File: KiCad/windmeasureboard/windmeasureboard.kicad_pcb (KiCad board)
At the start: 2 copper layers, 3 parts, among them J1 ESQ-120-XX-X-D-XX, U1 TMS320F28379DPTPS

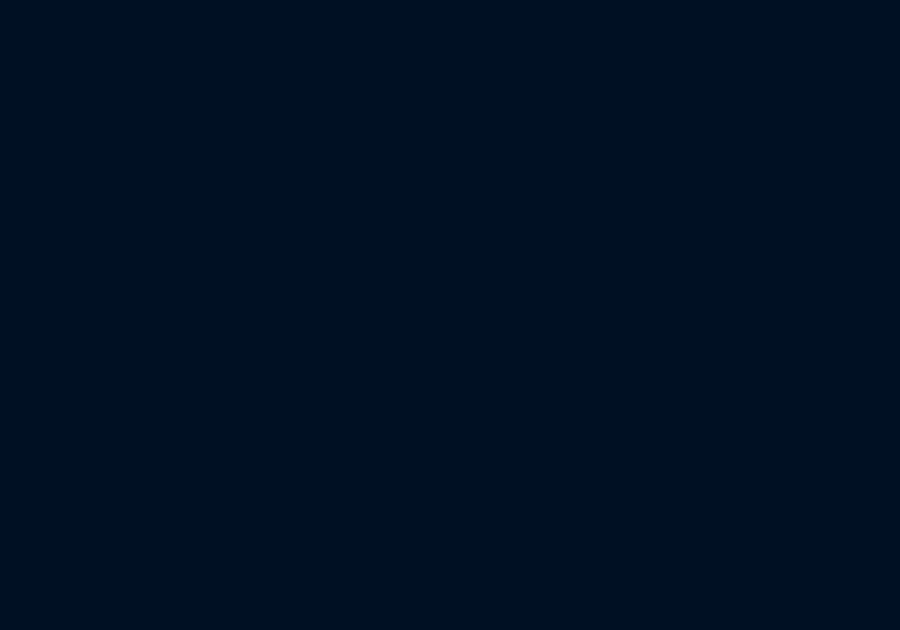
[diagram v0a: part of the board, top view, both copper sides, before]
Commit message: push before i swap out diodes for mosfets
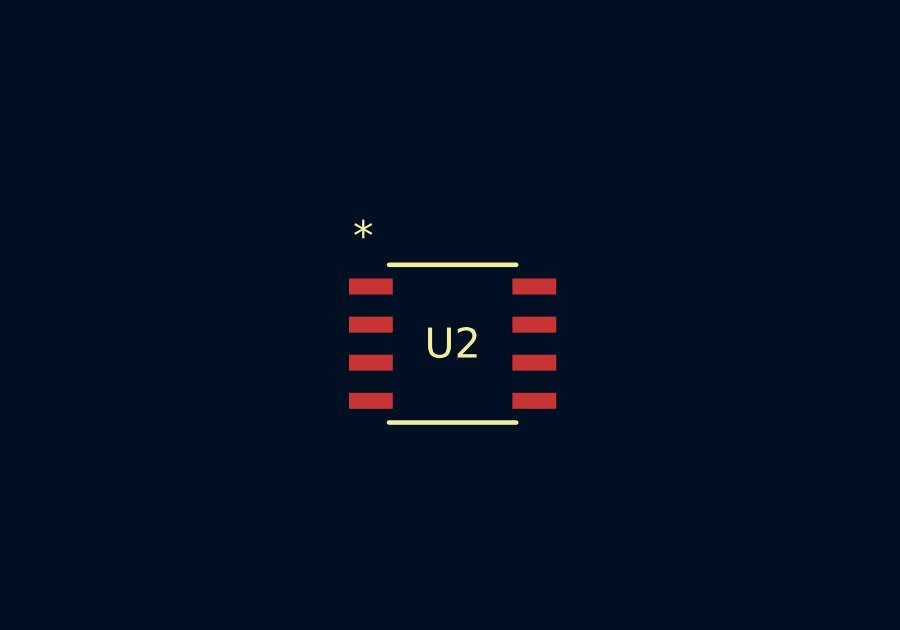
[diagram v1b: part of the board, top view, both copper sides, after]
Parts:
- added U2: LT1573IS8-PBF, footprints:SO-8_S_LIT, F.Cu at (131.9, 121.6)
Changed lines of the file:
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@@
   (net 213 "unconnected-(U1-Pad33)")
   (net 214 "unconnected-(U1-Pad45)")
+  (net 215 "unconnected-(U2-Pad1)")
+  (net 216 "unconnected-(U2-Pad2)")
+  (net 217 "unconnected-(U2-Pad3)")
+  (net 218 "unconnected-(U2-Pad4)")
+  (net 219 "unconnected-(U2-Pad5)")
+  (net 220 "unconnected-(U2-Pad6)")
+  (net 221 "unconnected-(U2-Pad7)")
+  (net 222 "unconnected-(U2-Pad8)")
   (footprint "footprints:PTP0176F_N" (layer "F.Cu")
     (at 133.532198 87.324401)
@@
       (net 1 "GND") (pinfunction "40") (pintype "passive") (solder_mask_margin 0.102))
   )
+  (footprint "footprints:SO-8_S_LIT" (layer "F.Cu")
+    (at 131.8514 121.6406)
+    (tags "LT1573IS8-PBF ")
+    (property "Sheetfile" "windmeasureboard.kicad_sch")
+    (property "Sheetname" "")
+    (attr smd)
+    (fp_text reference "U2" (at 0 0 unlocked) (layer "F.SilkS")
+      (effects (font (size 1 1) (thickness 0.15)))
+    )
+    (fp_text value "LT1573IS8-PBF" (at 0 0 unlocked) (layer "F.Fab")
+      (effects (font (size 1 1) (thickness 0.15)))
+    )
+    (fp_text user "*" (at -2.97815 -3.5814) (layer "F.SilkS")
+      (effects (font (size 1 1) (thickness 0.15)))
+    )
+    (fp_text user "*" (at -2.97815 -3.5814 unlocked) (layer "F.SilkS")
+      (effects (font (size 1 1) (thickness 0.15)))
+    )
+    (fp_text user "*" (at -1.6129 -2.4257 unlocked) (layer "F.Fab")
+      (effects (font (size 1 1) (thickness 0.15)))
+    )
+    (fp_text user "${REFERENCE}" (at 0 0 unlocked) (layer "F.Fab")
+      (effects (font (size 1 1) (thickness 0.15)))
+    )
+    (fp_text user "*" (at -1.6129 -2.4257) (layer "F.Fab")
+      (effects (font (size 1 1) (thickness 0.15)))
+    )
+    (fp_line (start 2.1209 -2.6289) (end -2.1209 -2.6289) (layer "F.SilkS") (width 0.1524))
+    (fp_line (start -2.1209 2.6289) (end 2.1209 2.6289) (layer "F.SilkS") (width 0.1524))
+    (fp_line (start -3.7084 -2.4257) (end -2.2479 -2.4257) (layer "F.CrtYd") (width 0.1524))
+    (fp_line (start 2.2479 2.4257) (end 2.2479 2.7559) (layer "F.CrtYd") (width 0.1524))
+    (fp_line (start -2.2479 2.7559) (end -2.2479 2.4257) (layer "F.CrtYd") (width 0.1524))
+    (fp_line (start 2.2479 -2.7559) (end 2.2479 -2.4257) (layer "F.CrtYd") (width 0.1524))
+    (fp_line (start -2.2479 -2.4257) (end -2.2479 -2.7559) (layer "F.CrtYd") (width 0.1524))
+    (fp_line (start 3.7084 2.4257) (end 2.2479 2.4257) (layer "F.CrtYd") (width 0.1524))
+    (fp_line (start -3.7084 2.4257) (end -2.2479 2.4257) (layer "F.CrtYd") (width 0.1524))
+    (fp_line (start 3.7084 -2.4257) (end 3.7084 2.4257) (layer "F.CrtYd") (width 0.1524))
+    (fp_line (start -3.7084 2.4257) (end -3.7084 -2.4257) (layer "F.CrtYd") (width 0.1524))
+    (fp_line (start 3.7084 -2.4257) (end 2.2479 -2.4257) (layer "F.CrtYd") (width 0.1524))
+    (fp_line (start 2.2479 2.7559) (end -2.2479 2.7559) (layer "F.CrtYd") (width 0.1524))
+    (fp_line (start -2.2479 -2.7559) (end 2.2479 -2.7559) (layer "F.CrtYd") (width 0.1524))
+    (fp_line (start 1.9939 -1.6637) (end 3.0988 -1.6637) (layer "F.Fab") (width 0.0254))
+    (fp_line (start -1.9939 0.8763) (end -1.9939 0.3937) (layer "F.Fab") (width 0.0254))
+    (fp_line (start 3.0988 0.8763) (end 3.0988 0.3937) (layer "F.Fab") (width 0.0254))
+    (fp_line (start -3.0988 1.6637) (end -3.0988 2.1463) (layer "F.Fab") (width 0.0254))
+    (fp_line (start 1.9939 1.6637) (end 1.9939 2.1463) (layer "F.Fab") (width 0.0254))
+    (fp_line (start -1.9939 -2.1463) (end -3.0988 -2.1463) (layer "F.Fab") (width 0.0254))
+    (fp_line (start -1.9939 -2.5019) (end -1.9939 2.5019) (layer "F.Fab") (width 0.0254))
+    (fp_line (start -3.0988 -0.3937) (end -1.9939 -0.3937) (layer "F.Fab") (width 0.0254))
+    (fp_line (start -1.9939 -1.6637) (end -1.9939 -2.1463) (layer "F.Fab") (width 0.0254))
+    (fp_line (start 1.9939 -2.1463) (end 1.9939 -1.6637) (layer "F.Fab") (width 0.0254))
+    (fp_line (start -1.9939 1.6637) (end -3.0988 1.6637) (layer "F.Fab") (width 0.0254))
+    (fp_line (start -3.0988 2.1463) (end -1.9939 2.1463) (layer "F.Fab") (width 0.0254))
+    (fp_line (start 1.9939 2.1463) (end 3.0988 2.1463) (layer "F.Fab") (width 0.0254))
+    (fp_line (start 1.9939 0.8763) (end 3.0988 0.8763) (layer "F.Fab") (width 0.0254))
+    (fp_line (start -1.9939 2.5019) (end 1.9939 2.5019) (layer "F.Fab") (width 0.0254))
+    (fp_line (start -3.0988 0.3937) (end -3.0988 0.8763) (layer "F.Fab") (width 0.0254))
+    (fp_line (start 3.0988 -0.8763) (end 1.9939 -0.8763) (layer "F.Fab") (width 0.0254))
+    (fp_line (start -1.9939 -0.3937) (end -1.9939 -0.8763) (layer "F.Fab") (width 0.0254))
+    (fp_line (start 3.0988 1.6637) (end 1.9939 1.6637) (layer "F.Fab") (width 0.0254))
+    (fp_line (start 3.0988 -2.1463) (end 1.9939 -2.1463) (layer "F.Fab") (width 0.0254))
+    (fp_line (start 1.9939 0.3937) (end 1.9939 0.8763) (layer "F.Fab") (width 0.0254))
+    (fp_line (start -3.0988 -0.8763) (end -3.0988 -0.3937) (layer "F.Fab") (width 0.0254))
+    (fp_line (start -3.0988 0.8763) (end -1.9939 0.8763) (layer "F.Fab") (width 0.0254))
+    (fp_line (start -1.9939 2.1463) (end -1.9939 1.6637) (layer "F.Fab") (width 0.0254))
+    (fp_line (start -1.9939 0.3937) (end -3.0988 0.3937) (layer "F.Fab") (width 0.0254))
+    (fp_line (start 1.9939 -0.3937) (end 3.0988 -0.3937) (layer "F.Fab") (width 0.0254))
+    (fp_line (start 1.9939 -2.5019) (end -1.9939 -2.5019) (layer "F.Fab") (width 0.0254))
+    (fp_line (start 3.0988 -0.3937) (end 3.0988 -0.8763) (layer "F.Fab") (width 0.0254))
+    (fp_line (start 1.9939 -0.8763) (end 1.9939 -0.3937) (layer "F.Fab") (width 0.0254))
+    (fp_line (start -3.0988 -1.6637) (end -1.9939 -1.6637) (layer "F.Fab") (width 0.0254))
+    (fp_line (start 3.0988 -1.6637) (end 3.0988 -2.1463) (layer "F.Fab") (width 0.0254))
+    (fp_line (start -1.9939 -0.8763) (end -3.0988 -0.8763) (layer "F.Fab") (width 0.0254))
+    (fp_line (start 1.9939 2.5019) (end 1.9939 -2.5019) (layer "F.Fab") (width 0.0254))
+    (fp_line (start -3.0988 -2.1463) (end -3.0988 -1.6637) (layer "F.Fab") (width 0.0254))
+    (fp_line (start 3.0988 0.3937) (end 1.9939 0.3937) (layer "F.Fab") (width 0.0254))
+    (fp_line (start 3.0988 2.1463) (end 3.0988 1.6637) (layer "F.Fab") (width 0.0254))
+    (fp_arc (start 0.3048 -2.5019) (mid 0 -2.1971) (end -0.3048 -2.5019) (layer "F.Fab") (width 0.0254))
+    (pad "1" smd rect (at -2.72415 -1.905) (size 1.4605 0.5334) (layers "F.Cu" "F.Paste" "F.Mask")
+      (net 215 "unconnected-(U2-Pad1)") (pinfunction "FB") (pintype "input"))
+    (pad "2" smd rect (at -2.72415 -0.635) (size 1.4605 0.5334) (layers "F.Cu" "F.Paste" "F.Mask")
+      (net 216 "unconnected-(U2-Pad2)") (pinfunction "LATCH") (pintype "unspecified"))
+    (pad "3" smd rect (at -2.72415 0.635) (size 1.4605 0.5334) (layers "F.Cu" "F.Paste" "F.Mask")
+      (net 217 "unconnected-(U2-Pad3)") (pinfunction "SHDN") (pintype "output"))
+    (pad "4" smd rect (at -2.72415 1.905) (size 1.4605 0.5334) (layers "F.Cu" "F.Paste" "F.Mask")
+      (net 218 "unconnected-(U2-Pad4)") (pinfunction "GND") (pintype "power_in"))
+    (pad "5" smd rect (at 2.72415 1.905) (size 1.4605 0.5334) (layers "F.Cu" "F.Paste" "F.Mask")
+      (net 219 "unconnected-(U2-Pad5)") (pinfunction "DRIVE") (pintype "unspecified"))
+    (pad "6" smd rect (at 2.72415 0.635) (size 1.4605 0.5334) (layers "F.Cu" "F.Paste" "F.Mask")
+      (net 220 "unconnected-(U2-Pad6)") (pinfunction "VIN") (pintype "input"))
+    (pad "7" smd rect (at 2.72415 -0.635) (size 1.4605 0.5334) (layers "F.Cu" "F.Paste" "F.Mask")
+      (net 221 "unconnected-(U2-Pad7)") (pinfunction "VOUT") (pintype "output"))
+    (pad "8" smd rect (at 2.72415 -1.905) (size 1.4605 0.5334) (layers "F.Cu" "F.Paste" "F.Mask")
+      (net 222 "unconnected-(U2-Pad8)") (pinfunction "COMP") (pintype "unspecified"))
+  )
   (footprint "footprints:CAPC3225X270N" (layer "F.Cu")

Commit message: worked on measure board
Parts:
- removed C1: GRM32EC72A106KE05L, footprints:CAPC3225X270N
- added LED1: XZMG56W, footprints:LED_XZMG56W_SLD, F.Cu at (125.0, 70.5)
- added LED2: XZMG56W, footprints:LED_XZMG56W_SLD, F.Cu at (121.1, 70.5)
- added LED3: XZMG56W, footprints:LED_XZMG56W_SLD, F.Cu at (117.2, 70.5)
- added LED4: XZMG56W, footprints:LED_XZMG56W_SLD, F.Cu at (113.1, 70.5)
- added LED5: XZMG56W, footprints:LED_XZMG56W_SLD, F.Cu at (109.1, 70.5)
- added LED6: XZMG56W, footprints:LED_XZMG56W_SLD, F.Cu at (105.1, 70.5)
- U1: value TMS320F28379DPTPS -> ESP32-S2-DEVKITC-1; footprint footprints:PTP0176F_N -> footprints:MODULE_ESP32-S2-DEVKITC-1
- U2: value LT1573IS8-PBF -> LM1084ISX-5.0_NOPB; footprint footprints:SO-8_S_LIT -> footprints:TS3B
- moved J1 58.1 mm to (130.0, 86.0)
- moved U2 56.4 mm to (165.6, 76.4)
- moved U1 37.8 mm to (131.8, 49.6), turned to 90 degrees
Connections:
- J1 pad 04: PhaseC- -> unconnected-(J1-Pad04)
- J1 pad 05: Brake_sig -> unconnected-(J1-Pad05)
- J1 pad 06: PhaseB- -> PhaseC-
- J1 pad 08: PhaseA- -> unconnected-(J1-Pad08)
- J1 pad 10: unconnected-(J1-Pad10) -> PhaseB-
- J1 pad 13: Shunt1 -> Brake_Q4
- J1 pad 14: unconnected-(J1-Pad14) -> PhaseA-
- J1 pad 15: Shunt2 -> Brake_Q1
- J1 pad 17: unconnected-(J1-Pad17) -> Brake_Q3
- J1 pad 19: unconnected-(J1-Pad19) -> Brake_Q2
- J1 pad 21: unconnected-(J1-Pad21) -> Brake_Q5
- J1 pad 23: unconnected-(J1-Pad23) -> Brake_Q6
- J1 pad 25: unconnected-(J1-Pad25) -> Shunt1
- J1 pad 26: unconnected-(J1-Pad26) -> PowerSW2
- J1 pad 27: unconnected-(J1-Pad27) -> Shunt2
- J1 pad 28: PowerSW2 -> PowerSW1
- J1 pad 29: unconnected-(J1-Pad29) -> Vdrive
- J1 pad 30: PowerSW1 -> Shunt8
- J1 pad 31: Vdrive -> PWM_sig
- J1 pad 32: Shunt8 -> Shunt7
- J1 pad 33: PWM_sig -> Shunt3
- J1 pad 34: Shunt7 -> unconnected-(J1-Pad34)
- J1 pad 35: Shunt3 -> Shunt4
- J1 pad 36: Shunt6 -> Shunt5
- J1 pad 37: Shunt4 -> unconnected-(J1-Pad37)
- J1 pad 38: Shunt5 -> unconnected-(J1-Pad38)
- J1 pad 40: GND -> Shunt6
- U2 pad 1: unconnected-(U2-Pad1) -> GND
- U2 pad 2: unconnected-(U2-Pad2) -> Vsupp
- U2 pad 3: unconnected-(U2-Pad3) -> Shunt6
- U2 pad 4: unconnected-(U2-Pad4) -> Shunt6
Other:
- board outline added: 103.8 x 61.2 mm
- board text added: "(VSupp)"
- board text added: "GND"
- board text added: "NC"
- board text added: "P1Out"
- board text added: "P2Out"
- board text added: "PGND"
- board text added: "PWM"
- board text added: "P_SW1"
- board text added: "P_SW2"
- board text added: "PhaseA"
- board text added: "PhaseA-"
- board text added: "PhaseB"
- board text added: "PhaseB-"
- board text added: "PhaseC"
- board text added: "PhaseC-"
- board text added: "Shunt1"
- board text added: "Shunt2"
- board text added: "Shunt3"
- board text added: "Shunt4"
- board text added: "Shunt5"
- board text added: "Shunt7"
- board text added: "Vdrive"
- board text added: "WMB V.1.0 K.Q"
- board text added: "brakeQ1"
- board text added: "brakeQ2"
- board text added: "brakeQ3"
- board text added: "brakeQ4"
- board text added: "brakeQ5"
- board text added: "brakeQ6"

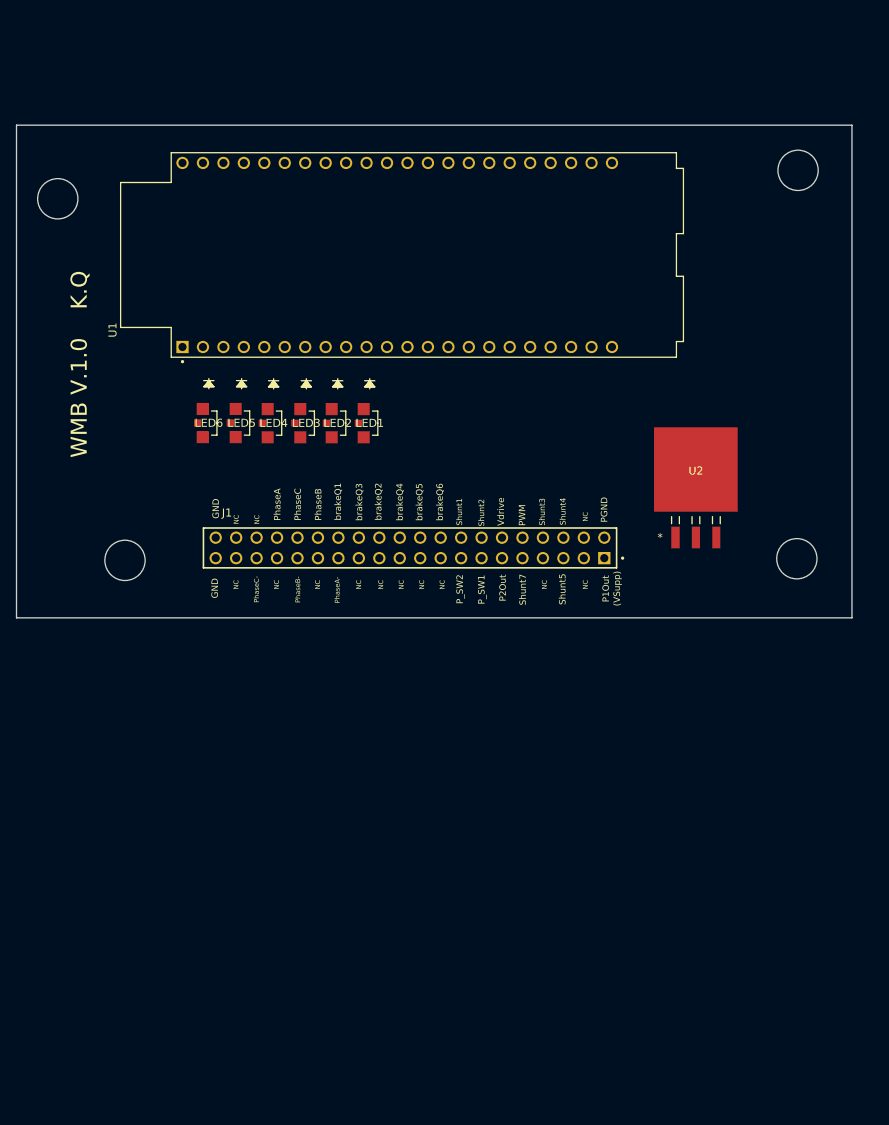
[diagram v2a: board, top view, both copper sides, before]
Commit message: V1 Measure Board Finished
Also started manual data collection for turbine and started updating files to kicad V7
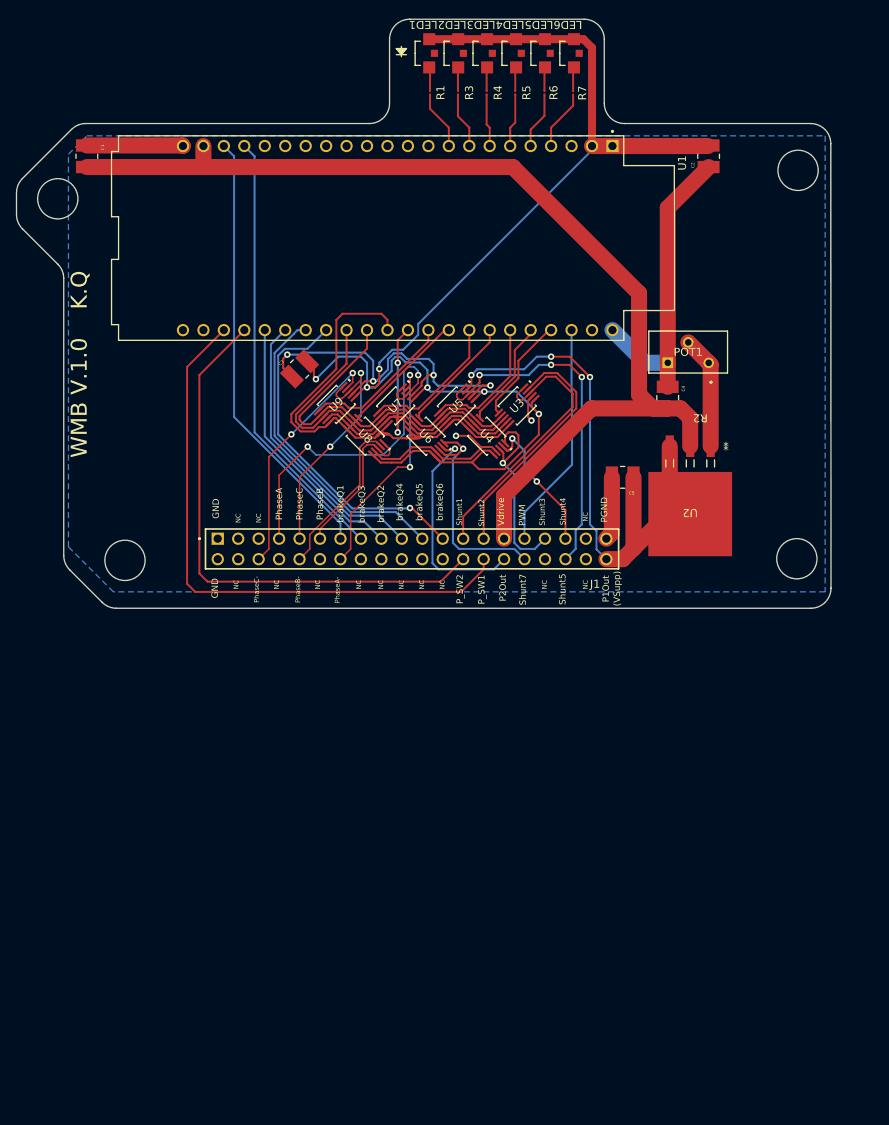
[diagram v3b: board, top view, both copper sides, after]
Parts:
- added C1: GRM32EC72A106KE05L, footprints:CAPC3225X270N, F.Cu at (89.9, 37.3)
- added C2: GRM32EC72A106KE05L, footprints:CAPC3225X270N, F.Cu at (167.1, 37.3)
- added C3: GRM32EC72A106KE05L, footprints:CAPC3225X270N, F.Cu at (116.3, 63.8)
- added C4: GRM32EC72A106KE05L, footprints:CAPC3225X270N, F.Cu at (162.1, 67.3)
- added C5: GRM32EC72A106KE05L, footprints:CAPC3225X270N, F.Cu at (156.5, 77.2)
- added POT1: 3296Y-1-502LF, footprints:POT_3296Y, F.Cu at (162.1, 63.0)
- added R1: ERJXGNJ560Y, footprints:ERJXGN_RCD, F.Cu at (132.5, 29.4)
- added R2: CRCW04021K00FKED, footprints:RES_CRCW_0402, F.Cu at (166.1, 69.8)
- added R3: ERJXGNJ560Y, footprints:ERJXGN_RCD, F.Cu at (136.0, 29.4)
- added R4: ERJXGNJ560Y, footprints:ERJXGN_RCD, F.Cu at (139.6, 29.4)
- added R5: ERJXGNJ560Y, footprints:ERJXGN_RCD, F.Cu at (143.1, 29.4)
- added R6: ERJXGNJ560Y, footprints:ERJXGN_RCD, F.Cu at (146.7, 29.4)
- added R7: ERJXGNJ560Y, footprints:ERJXGN_RCD, F.Cu at (150.3, 29.5)
- added U3: INA229AIDGSR, footprints:VSSOP10_DGS_TEX, F.Cu at (143.4, 68.3)
- added U4: INA229AIDGSR, footprints:VSSOP10_DGS_TEX, F.Cu at (139.6, 72.1)
- added U5: INA229AIDGSR, footprints:VSSOP10_DGS_TEX, F.Cu at (135.8, 68.3)
- added U6: INA229AIDGSR, footprints:VSSOP10_DGS_TEX, F.Cu at (132.0, 72.1)
- added U7: INA229AIDGSR, footprints:VSSOP10_DGS_TEX, F.Cu at (128.3, 68.3)
- added U8: INA229AIDGSR, footprints:VSSOP10_DGS_TEX, F.Cu at (124.5, 72.1)
- added U9: INA229AIDGSR, footprints:VSSOP10_DGS_TEX, F.Cu at (120.9, 68.2)
- moved LED6 64.0 mm to (149.7, 24.6), turned to 180 degrees
- moved LED5 58.9 mm to (146.1, 24.6), turned to 180 degrees
- moved LED4 54.5 mm to (142.5, 24.6), turned to 180 degrees
- moved LED3 50.8 mm to (138.9, 24.6), turned to 180 degrees
- moved LED2 48.1 mm to (135.3, 24.6), turned to 180 degrees
- moved LED1 46.4 mm to (131.7, 24.6), turned to 180 degrees
- moved U1 6.87 mm to (125.2, 47.5), turned to -90 degrees
- moved U2 5.27 mm to (164.8, 81.6), turned to 180 degrees
- moved J1 0.28 mm to (130.3, 86.1), turned to 180 degrees
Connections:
- LED1 pad 1: LED1 -> Net-(LED1-Pad1)
- LED2 pad 1: LED2 -> Net-(LED2-Pad1)
- LED3 pad 1: LED3 -> Net-(LED3-Pad1)
- LED4 pad 1: LED4 -> Net-(LED4-Pad1)
- LED5 pad 1: LED5 -> Net-(LED5-Pad1)
- LED6 pad 1: LED6 -> Net-(LED6-Pad1)
- U1 pad J1_19: unconnected-(U1-PadJ1_19) -> Brake_Q1
- U1 pad J1_2: LED6 -> V3.3+
- U1 pad J1_20: unconnected-(U1-PadJ1_20) -> Brake_Q4
- U1 pad J1_21: Vsupp -> Vdrive
- U1 pad J1_3: LED5 -> unconnected-(U1-EN-PadJ1_3)
- U1 pad J1_4: LED4 -> LED6
- U1 pad J1_5: LED3 -> LED5
- U1 pad J1_6: LED2 -> LED4
- U1 pad J1_7: LED1 -> LED3
- U1 pad J1_8: unconnected-(U1-PadJ1_8) -> LED2
- U1 pad J1_9: unconnected-(U1-PadJ1_9) -> LED1
- U1 pad J3_10: unconnected-(U1-PadJ3_10) -> /measurement chips/CS7
- U1 pad J3_11: unconnected-(U1-PadJ3_11) -> /measurement chips/MISO
- U1 pad J3_12: unconnected-(U1-PadJ3_12) -> /measurement chips/SCLK
- U1 pad J3_13: unconnected-(U1-PadJ3_13) -> /measurement chips/MOSI
- U1 pad J3_14: unconnected-(U1-PadJ3_14) -> /measurement chips/ALERT
- U1 pad J3_15: unconnected-(U1-PadJ3_15) -> Brake_Q6
- U1 pad J3_16: unconnected-(U1-PadJ3_16) -> Brake_Q5
- U1 pad J3_17: unconnected-(U1-PadJ3_17) -> Brake_Q2
- U1 pad J3_18: unconnected-(U1-PadJ3_18) -> Brake_Q3
- U1 pad J3_19: unconnected-(U1-PadJ3_19) -> PowerSW2
- U1 pad J3_20: unconnected-(U1-PadJ3_20) -> PowerSW1
- U1 pad J3_3: unconnected-(U1-PadJ3_3) -> PWM_sig
- U1 pad J3_4: unconnected-(U1-PadJ3_4) -> /measurement chips/CS1
- U1 pad J3_5: unconnected-(U1-PadJ3_5) -> /measurement chips/CS2
- U1 pad J3_6: unconnected-(U1-PadJ3_6) -> /measurement chips/CS3
- U1 pad J3_7: unconnected-(U1-PadJ3_7) -> /measurement chips/CS4
- U1 pad J3_8: unconnected-(U1-PadJ3_8) -> /measurement chips/CS5
- U1 pad J3_9: unconnected-(U1-PadJ3_9) -> /measurement chips/CS6
- U2 pad 1: GND -> Net-(U2-ADJ/GND)
- U2 pad 2: Vsupp -> Vdrive
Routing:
- net V3.3+: track 0.00 -> 174.9 mm, vias 0 -> 6
- net Vdrive: track 0.00 -> 131.6 mm
- net GND: track 0.00 -> 130.7 mm, vias 0 -> 6
- net Shunt6: track 0.00 -> 73.4 mm, vias 0 -> 3
- net PowerSW1: track 0.00 -> 73.1 mm
- net PowerSW2: track 0.00 -> 67.6 mm
- net /measurement chips/SCLK: track 0.00 -> 58.9 mm
- net Brake_Q1: track 0.00 -> 54.9 mm
- net Brake_Q4: track 0.00 -> 54.8 mm
- net /measurement chips/ALERT: track 0.00 -> 46.3 mm
- net /measurement chips/MOSI: track 0.00 -> 45.9 mm
- net Shunt5: track 0.00 -> 43.7 mm, vias 0 -> 3
- net /measurement chips/MISO: track 0.00 -> 43.1 mm, vias 0 -> 2
- net PhaseA+: track 0.00 -> 43.0 mm, vias 0 -> 2
- net Brake_Q6: track 0.00 -> 42.9 mm, vias 0 -> 1
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- added copper zone on F.Cu, net /measurement chips/MISO
- added copper zone on F.Cu, net /measurement chips/SCLK
- added copper zone on B.Cu, net GND
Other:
- board size 103.8 x 61.2 mm -> 101.2 x 73.2 mm
